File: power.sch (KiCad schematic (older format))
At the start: 24 parts

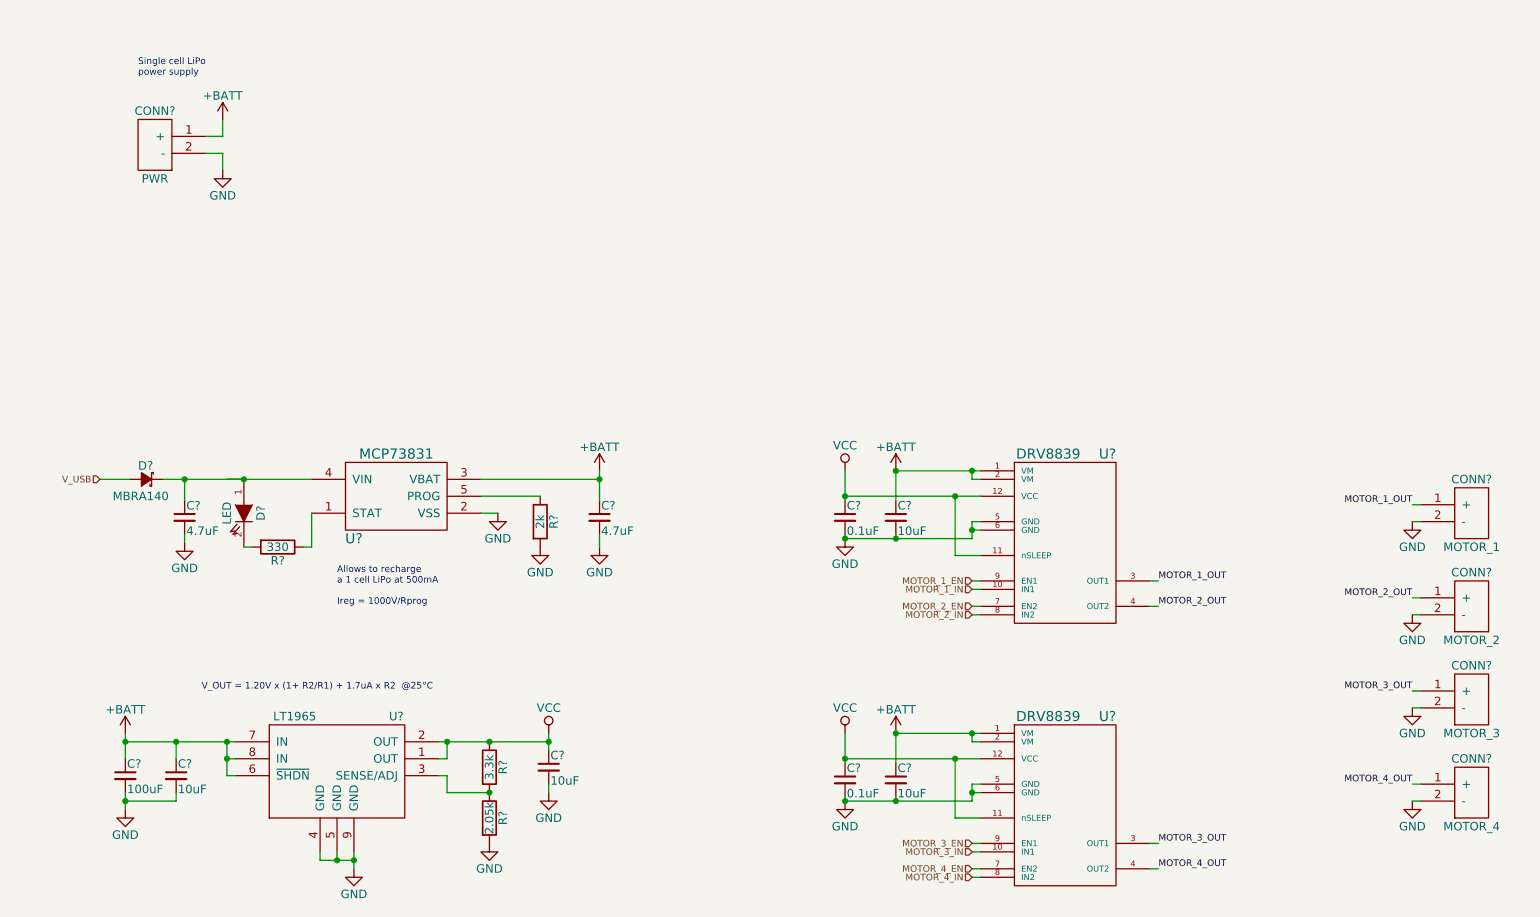
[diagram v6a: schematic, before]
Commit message: Add pushbutton power management
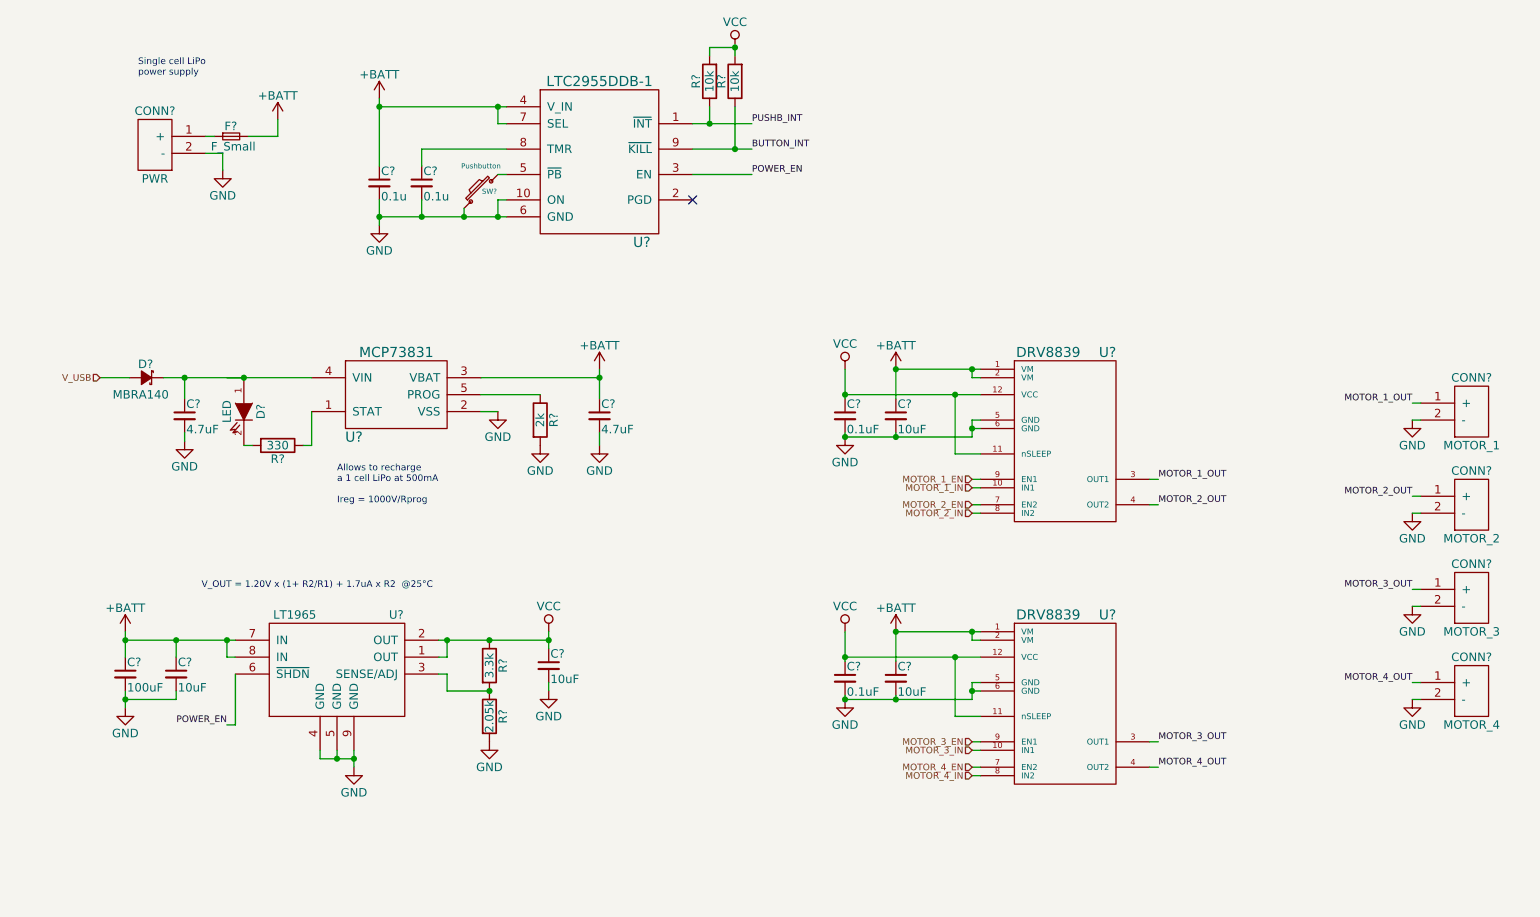
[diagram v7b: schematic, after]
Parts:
- added C? (x2): 0.1u, symbol C_Small
- added F?: F_Small, symbol F_Small
- added R? (x2): 10k, symbol R
- added SW?: Pushbutton, symbol SW_PUSH_SMALL
- added U?: LTC2955DDB-1, symbol LTC2955DDB-1
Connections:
- net +BATT: now also C?.1, F?.2, U?.4 (V_IN), U?.7 (SEL); no longer CONN?.1 (+), U?.6 (~SHDN)
- net GND: now also C?.2, C?.2, SW?.1, U?.10 (ON), U?.6 (GND)
- net VCC: now also R?.2, R?.2
- new net: CONN?.1 (+), F?.1
- new net: SW?.2, U?.5 (~PB)
- new net: C?.1, U?.8 (TMR)
- new net BUTTON_INT: R?.1, U?.9 (~KILL)
- new net POWER_EN: U?.3 (EN), U?.6 (~SHDN)
- new net PUSHB_INT: R?.1, U?.1 (~INT)
- no-connect marks 0 -> 1
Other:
- moved on the sheet: C?, CONN?, D?, R?, U?

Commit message: Add IR Leds on top and bottom with enable on MCU
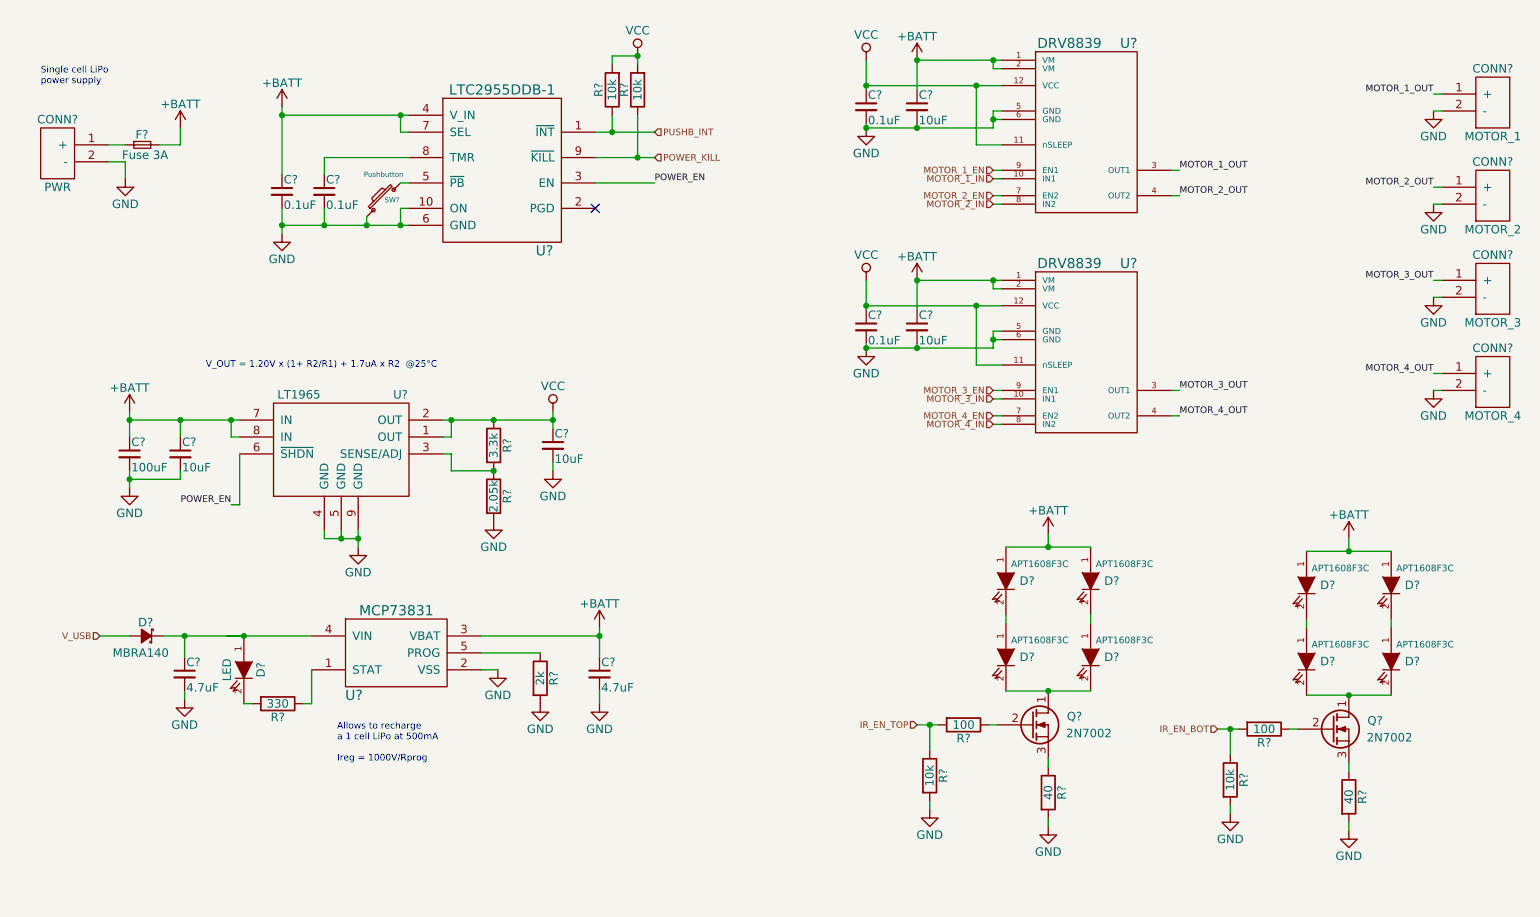
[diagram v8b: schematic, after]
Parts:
- added D? (x8): APT1608F3C, symbol LED
- added Q? (x2): 2N7002, symbol Q_NMOS_DGS
- added R? (x2): 40, symbol R
- added R? (x2): 100, symbol R
- added R? (x2): 10k, symbol R
- C? (x2): value 0.1u -> 0.1uF
- F?: value F_Small -> Fuse 3A
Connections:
- net +BATT: now also D?.1 (A), D?.1 (A), D?.1 (A), D?.1 (A)
- net GND: now also R?.2, R?.2, R?.2, R?.2
- net BUTTON_INT renamed POWER_KILL
- new net: D?.1 (A), D?.2 (K) (x4)
- new net: D?.2 (K), D?.2 (K), Q?.1 (D) (x2)
- new net: Q?.2 (G), R?.1 (x2)
- new net: Q?.3 (S), R?.1 (x2)
- new net IR_EN_BOT: R?.1, R?.2
- new net IR_EN_TOP: R?.1, R?.2
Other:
- moved on the sheet: C?, CONN?, D?, F?, R?, SW?, U?
